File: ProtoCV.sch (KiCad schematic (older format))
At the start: 107 parts, among them J1 AudioJack2_SwitchT, J10 Conn_01x09_Male, J11 Conn_01x05_Male, J12 Conn_01x09_Male, J13 AudioJack2_SwitchT, J14 AudioJack2_SwitchT, J15 AudioJack2_SwitchT, J16 AudioJack2_SwitchT, J17 AudioJack2_SwitchT, J18 AudioJack2_SwitchT, J19 AudioJack2_SwitchT, J2 AudioJack2_SwitchT, J20 AudioJack2_SwitchT, J3 AudioJack2_SwitchT, J4 AudioJack2_SwitchT, J5 AudioJack2_SwitchT, J6 AudioJack2_SwitchT, J7 AudioJack2_SwitchT, J8 AudioJack2_SwitchT, J9 Conn_02x05_Odd_Even, U1 OPA4192, U2 OPA4192, U3 DC80508Z, U4 R-78E3.3-0.5, U5 LD2981ABU33TR, U6 74AHCT244, U7 L7805

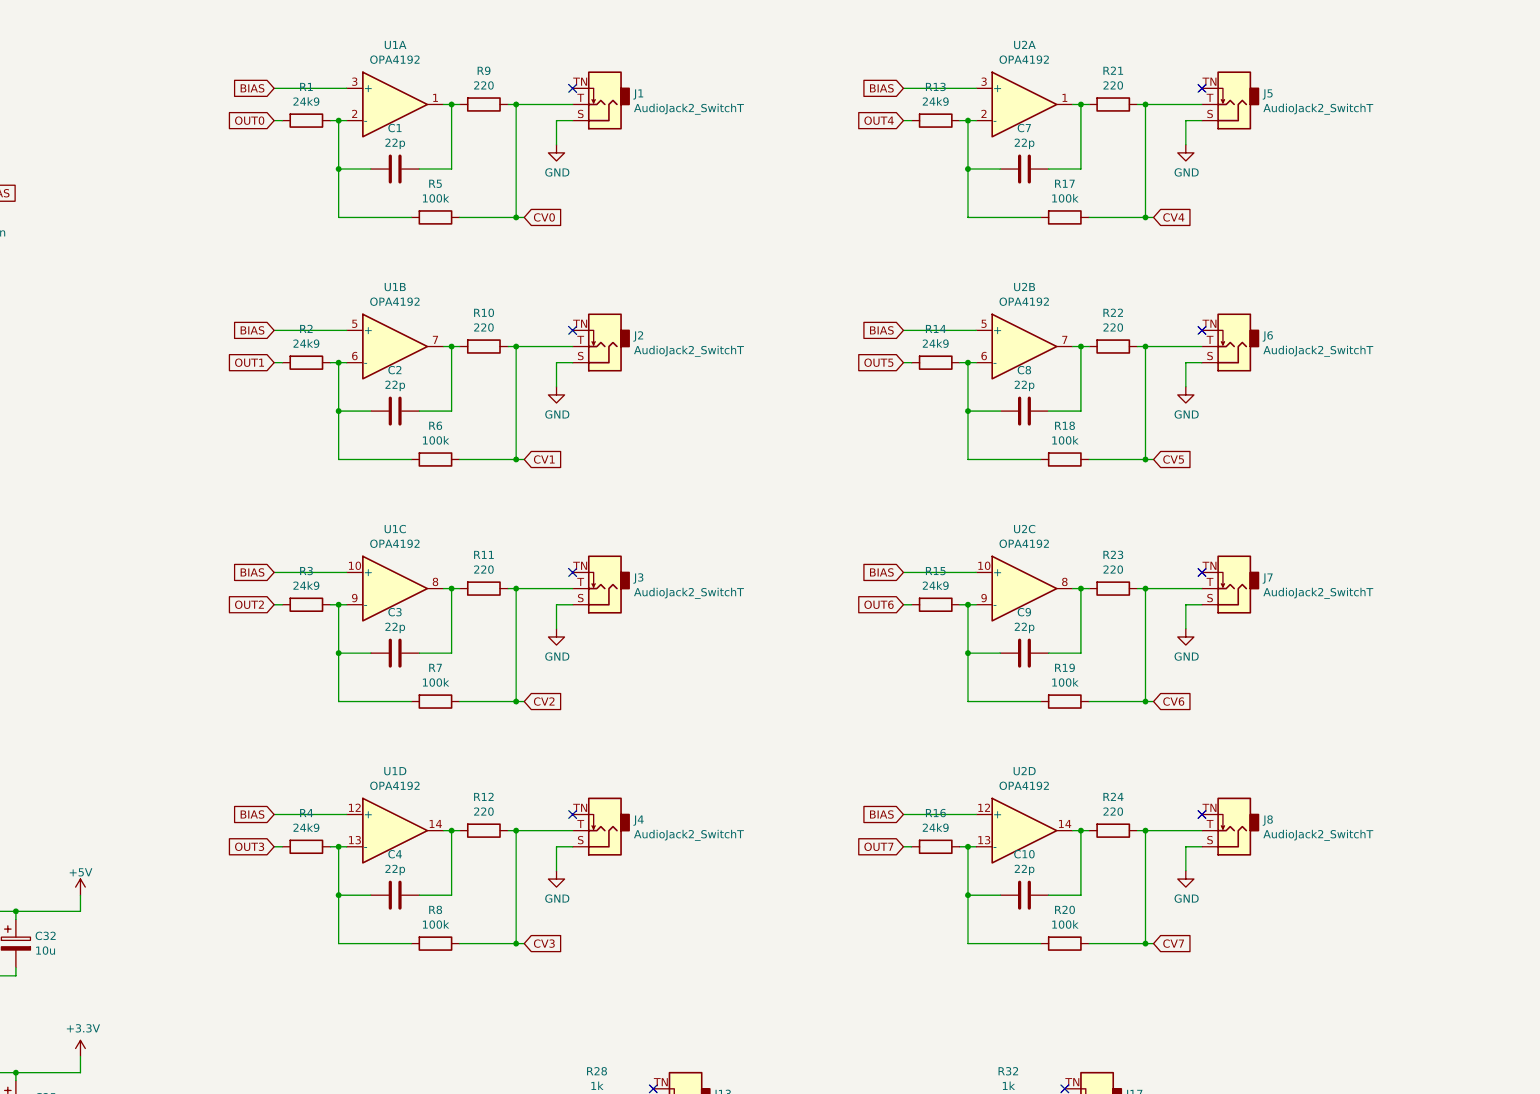
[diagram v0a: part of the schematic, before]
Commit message: Added leds and drivers.
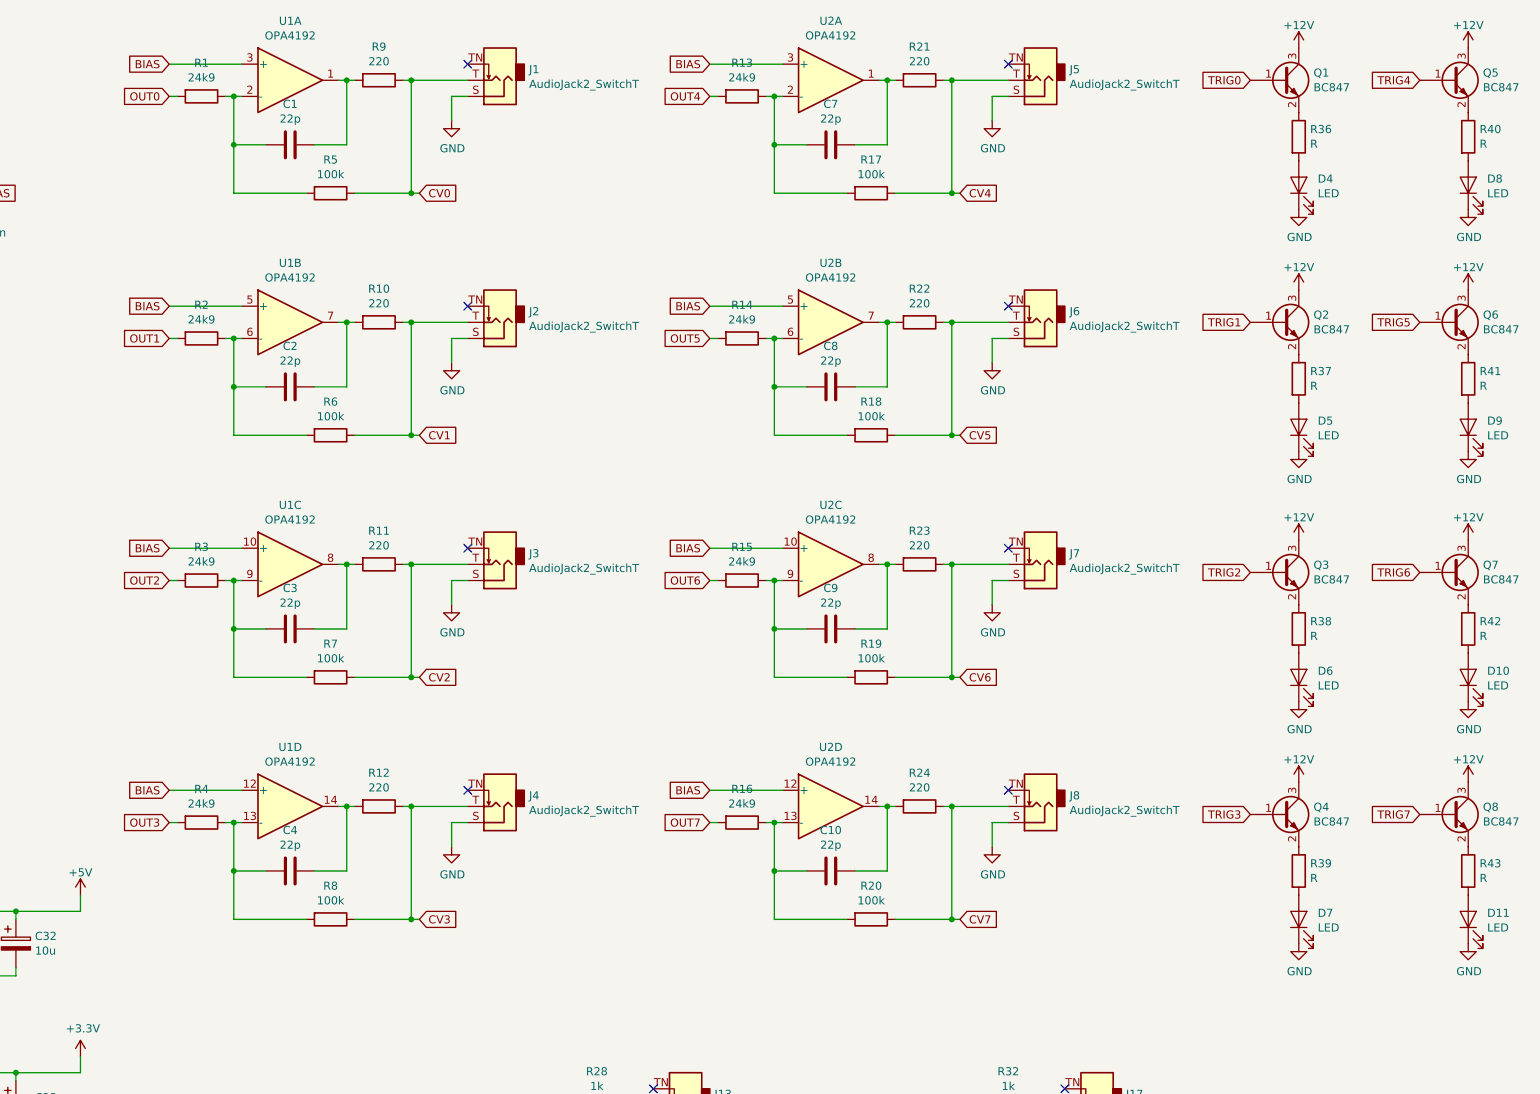
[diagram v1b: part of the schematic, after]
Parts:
- added D10, D11, D4, D5, D6, D7, D8, D9: LED, symbol Device:LED
- added Q1, Q2, Q3, Q4, Q5, Q6, Q7, Q8: BC847, Package_TO_SOT_SMD:SOT-23, symbol Transistor_BJT:BC847
- added R36, R37, R38, R39, R40, R41, R42, R43: R, symbol Device:R
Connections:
- net +12V: now also Q1.3 (C), Q2.3 (C), Q3.3 (C), Q4.3 (C), Q5.3 (C), Q6.3 (C), Q7.3 (C), Q8.3 (C)
- net GND: now also D10.1 (K), D11.1 (K), D4.1 (K), D5.1 (K), D6.1 (K), D7.1 (K), D8.1 (K), D9.1 (K)
- net TRIG0: now also Q1.1 (B)
- net TRIG1: now also Q2.1 (B)
- net TRIG2: now also Q3.1 (B)
- net TRIG3: now also Q4.1 (B)
- net TRIG4: now also Q5.1 (B)
- net TRIG5: now also Q6.1 (B)
- net TRIG6: now also Q7.1 (B)
- net TRIG7: now also Q8.1 (B)
- new net: Q1.2 (E), R36.1
- new net: D4.2 (A), R36.2
- new net: Q5.2 (E), R40.1
- new net: D8.2 (A), R40.2
- new net: Q2.2 (E), R37.1
- new net: D5.2 (A), R37.2
- new net: Q6.2 (E), R41.1
- new net: D9.2 (A), R41.2
- new net: Q3.2 (E), R38.1
- new net: D6.2 (A), R38.2
- new net: Q7.2 (E), R42.1
- new net: D10.2 (A), R42.2
- new net: Q4.2 (E), R39.1
- new net: D7.2 (A), R39.2
- new net: Q8.2 (E), R43.1
- new net: D11.2 (A), R43.2
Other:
- moved on the sheet: C1, C10, C2, C3, C4, C7, C8, C9, J1, J2, J3, J4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

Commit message: Assigned footprints.
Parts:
- C1, C10, C11, C12, C13, C14, C15, C2, C3, C4, C5, C6, C7, C8, C9: footprint (none) -> Capacitor_SMD:C_0603_1608Metric
- D10, D11, D4, D5, D6, D7, D8, D9: footprint (none) -> LED_SMD:LED_0603_1608Metric_Castellated
- H1, H2, H3, H4: footprint (none) -> MountingHole:MountingHole_3.2mm_M3_Pad_Via
- J1, J2, J3, J4, J5, J6, J7, J8: footprint (none) -> Local:PJ398SM
- J10, J12: footprint (none) -> Connector_PinHeader_2.54mm:PinHeader_1x09_P2.54mm_Vertical
- J11: footprint (none) -> Connector_PinHeader_2.54mm:PinHeader_1x05_P2.54mm_Vertical
- R1, R13, R14, R15, R16, R17, R18, R19, R2, R20, R25, R26, R3, R4, R5, R6, R7, R8: footprint (none) -> Resistor_SMD:R_0603_1608Metric
- R10, R11, R12, R21, R22, R23, R24, R9: footprint (none) -> Resistor_SMD:R_1206_3216Metric
- R36, R37, R38, R39, R40, R41, R42, R43: value R -> 47; footprint (none) -> Resistor_SMD:R_0603_1608Metric
- U1, U2: footprint (none) -> Package_SO:TSSOP-14_4.4x5mm_P0.65mm
- U3: value DC80508Z -> ADC80508Z; footprint (none) -> Package_DFN_QFN:QFN-16-1EP_3x3mm_P0.5mm_EP1.45x1.45mm_ThermalVias; symbol Local:DC80508Z -> Local:ADC80508Z

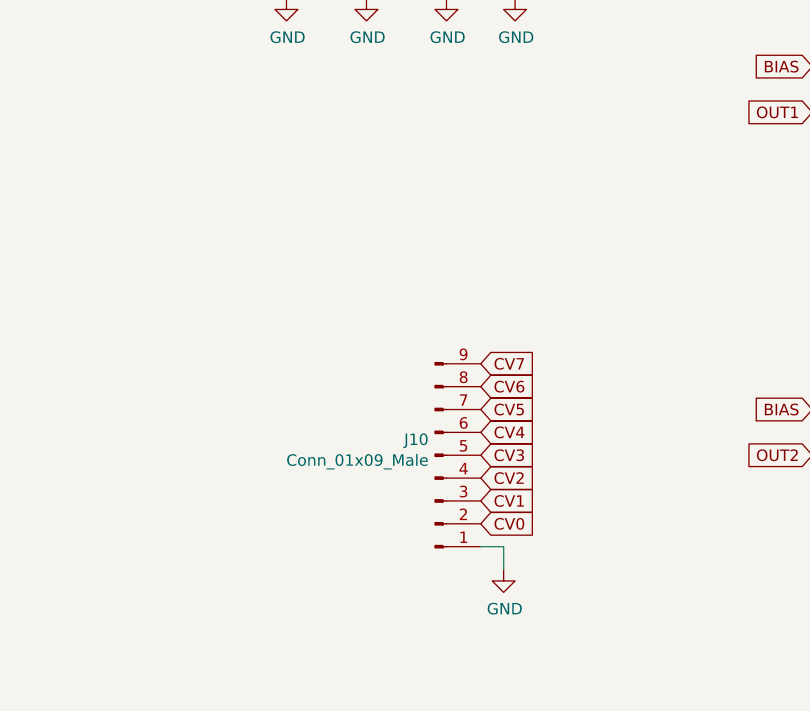
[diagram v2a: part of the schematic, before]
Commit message: Starting placement.
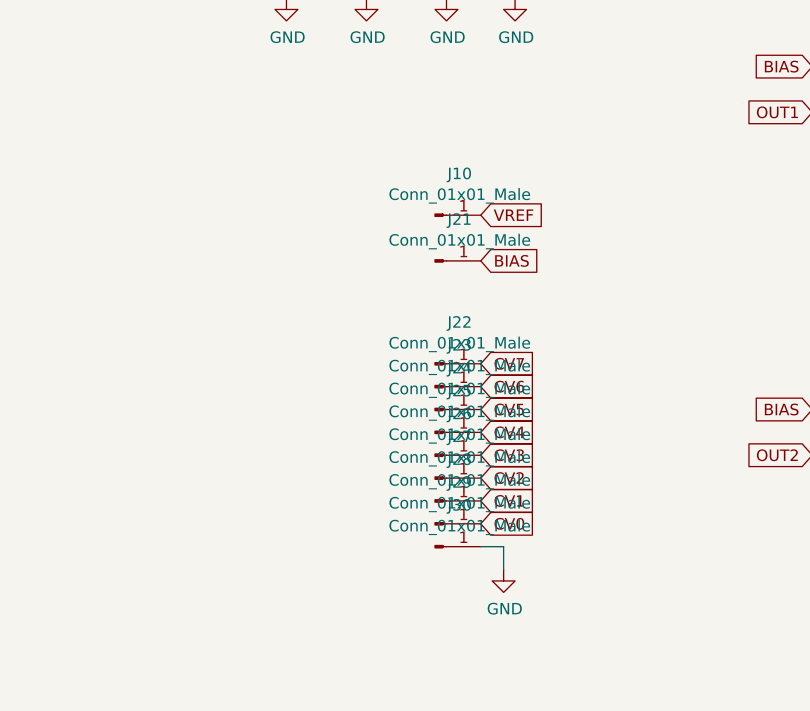
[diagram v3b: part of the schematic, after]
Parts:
- removed J10: Conn_01x09_Male, Connector_PinHeader_2.54mm:PinHeader_1x09_P2.54mm_Vertical, symbol Connector:Conn_01x09_Male
- added J10, J21, J22, J23, J24, J25, J26, J27, J28, J29, J30: Conn_01x01_Male, Connector_PinHeader_2.54mm:PinHeader_1x01_P2.54mm_Vertical, symbol Connector:Conn_01x01_Male
- J13, J14, J15, J16, J17, J18, J19, J20: footprint Local.pretty:PJ398SM -> Local:PJ398SM
- L1: footprint Inductor_SMD:L_0805_2012Metric -> Fuse:Fuse_Bourns_MF-RHT100
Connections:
- net BIAS: now also J21.1 (Pin_1)
- net CV0: now also J29.1 (Pin_1)
- net CV1: now also J28.1 (Pin_1)
- net CV2: now also J27.1 (Pin_1)
- net CV3: now also J26.1 (Pin_1)
- net CV4: now also J25.1 (Pin_1)
- net CV5: now also J24.1 (Pin_1)
- net CV6: now also J23.1 (Pin_1)
- net CV7: now also J22.1 (Pin_1)
- net GND: now also J30.1 (Pin_1)
- net VREF: now also J10.1 (Pin_1)
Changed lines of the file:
@@
 Connection ~ 12150 2100
-$Comp
-L Connector:Conn_01x09_Male J10
-U 1 1 5F278798
-P 5650 4500
-F 0 "J10" H 5622 4432 50  0000 R CNN
-F 1 "Conn_01x09_Male" H 5622 4523 50  0000 R CNN
-F 2 "Connector_PinHeader_2.54mm:PinHeader_1x09_P2.54mm_Vertical" H 5650 4500 50  0001 C CNN
-F 3 "~" H 5650 4500 50  0001 C CNN
-	1    5650 4500
-	1    0    0    1
-$EndComp
 $Comp
 L power:GND #PWR014
@@
 F 0 "L1" H 3900 7765 50  0000 C CNN
 F 1 "33u" H 3900 7674 50  0000 C CNN
-F 2 "Inductor_SMD:L_0805_2012Metric" H 3900 7550 50  0001 C CNN
+F 2 "Fuse:Fuse_Bourns_MF-RHT100" H 3900 7550 50  0001 C CNN
 F 3 "~" H 3900 7550 50  0001 C CNN
 	1    3900 7550
@@
 F 0 "J13" H 10321 7683 50  0000 R CNN
 F 1 "AudioJack2_SwitchT" H 10321 7774 50  0000 R CNN
-F 2 "Local.pretty:PJ398SM" H 10500 7750 50  0001 C CNN
+F 2 "Local:PJ398SM" H 10500 7750 50  0001 C CNN
 F 3 "~" H 10500 7750 50  0001 C CNN
 	1    10500 7750
@@
 F 0 "J14" H 10321 8133 50  0000 R CNN
 F 1 "AudioJack2_SwitchT" H 10321 8224 50  0000 R CNN
-F 2 "Local.pretty:PJ398SM" H 10500 8200 50  0001 C CNN
+F 2 "Local:PJ398SM" H 10500 8200 50  0001 C CNN
 F 3 "~" H 10500 8200 50  0001 C CNN
 	1    10500 8200
@@
 F 0 "J15" H 10321 8583 50  0000 R CNN
 F 1 "AudioJack2_SwitchT" H 10321 8674 50  0000 R CNN
-F 2 "Local.pretty:PJ398SM" H 10500 8650 50  0001 C CNN
+F 2 "Local:PJ398SM" H 10500 8650 50  0001 C CNN
 F 3 "~" H 10500 8650 50  0001 C CNN
 	1    10500 8650
@@
 F 0 "J16" H 10321 9033 50  0000 R CNN
 F 1 "AudioJack2_SwitchT" H 10321 9124 50  0000 R CNN
-F 2 "Local.pretty:PJ398SM" H 10500 9100 50  0001 C CNN
+F 2 "Local:PJ398SM" H 10500 9100 50  0001 C CNN
 F 3 "~" H 10500 9100 50  0001 C CNN
 	1    10500 9100
@@
 F 0 "J17" H 12871 7683 50  0000 R CNN
 F 1 "AudioJack2_SwitchT" H 12871 7774 50  0000 R CNN
-F 2 "Local.pretty:PJ398SM" H 13050 7750 50  0001 C CNN
+F 2 "Local:PJ398SM" H 13050 7750 50  0001 C CNN
 F 3 "~" H 13050 7750 50  0001 C CNN
 	1    13050 7750
@@
 F 0 "J18" H 12871 8133 50  0000 R CNN
 F 1 "AudioJack2_SwitchT" H 12871 8224 50  0000 R CNN
-F 2 "Local.pretty:PJ398SM" H 13050 8200 50  0001 C CNN
+F 2 "Local:PJ398SM" H 13050 8200 50  0001 C CNN
 F 3 "~" H 13050 8200 50  0001 C CNN
 	1    13050 8200
@@
 F 0 "J19" H 12871 8583 50  0000 R CNN
 F 1 "AudioJack2_SwitchT" H 12871 8674 50  0000 R CNN
-F 2 "Local.pretty:PJ398SM" H 13050 8650 50  0001 C CNN
+F 2 "Local:PJ398SM" H 13050 8650 50  0001 C CNN
 F 3 "~" H 13050 8650 50  0001 C CNN
 	1    13050 8650
@@
 F 0 "J20" H 12871 9033 50  0000 R CNN
 F 1 "AudioJack2_SwitchT" H 12871 9124 50  0000 R CNN
-F 2 "Local.pretty:PJ398SM" H 13050 9100 50  0001 C CNN
+F 2 "Local:PJ398SM" H 13050 9100 50  0001 C CNN
 F 3 "~" H 13050 9100 50  0001 C CNN
 	1    13050 9100
@@
 Text GLabel 15050 5950 0    50   Input ~ 0
 TRIG7
+$Comp
+L Connector:Conn_01x01_Male J22
+U 1 1 608E79F2
+P 5650 4100
+F 0 "J22" H 5758 4281 50  0000 C CNN
+F 1 "Conn_01x01_Male" H 5758 4190 50  0000 C CNN
+F 2 "Connector_PinHeader_2.54mm:PinHeader_1x01_P2.54mm_Vertical" H 5650 4100 50  0001 C CNN
+F 3 "~" H 5650 4100 50  0001 C CNN
+	1    5650 4100
+	1    0    0    -1
+$EndComp
+$Comp
+L Connector:Conn_01x01_Male J23
+U 1 1 608E967A
+P 5650 4200
+F 0 "J23" H 5758 4381 50  0000 C CNN
+F 1 "Conn_01x01_Male" H 5758 4290 50  0000 C CNN
+F 2 "Connector_PinHeader_2.54mm:PinHeader_1x01_P2.54mm_Vertical" H 5650 4200 50  0001 C CNN
+F 3 "~" H 5650 4200 50  0001 C CNN
+	1    5650 4200
+	1    0    0    -1
+$EndComp
+$Comp
+L Connector:Conn_01x01_Male J24
+U 1 1 608E9862
+P 5650 4300
+F 0 "J24" H 5758 4481 50  0000 C CNN
+F 1 "Conn_01x01_Male" H 5758 4390 50  0000 C CNN
+F 2 "Connector_PinHeader_2.54mm:PinHeader_1x01_P2.54mm_Vertical" H 5650 4300 50  0001 C CNN
+F 3 "~" H 5650 4300 50  0001 C CNN
+	1    5650 4300
+	1    0    0    -1
+$EndComp
+$Comp
+L Connector:Conn_01x01_Male J25
+U 1 1 608E9A83
+P 5650 4400
+F 0 "J25" H 5758 4581 50  0000 C CNN
+F 1 "Conn_01x01_Male" H 5758 4490 50  0000 C CNN
+F 2 "Connector_PinHeader_2.54mm:PinHeader_1x01_P2.54mm_Vertical" H 5650 4400 50  0001 C CNN
+F 3 "~" H 5650 4400 50  0001 C CNN
+	1    5650 4400
+	1    0    0    -1
+$EndComp
+$Comp
+L Connector:Conn_01x01_Male J26
+U 1 1 608E9C1A
+P 5650 4500
+F 0 "J26" H 5758 4681 50  0000 C CNN
+F 1 "Conn_01x01_Male" H 5758 4590 50  0000 C CNN
+F 2 "Connector_PinHeader_2.54mm:PinHeader_1x01_P2.54mm_Vertical" H 5650 4500 50  0001 C CNN
+F 3 "~" H 5650 4500 50  0001 C CNN
+	1    5650 4500
+	1    0    0    -1
+$EndComp
+$Comp
+L Connector:Conn_01x01_Male J27
+U 1 1 608E9F06
+P 5650 4600
+F 0 "J27" H 5758 4781 50  0000 C CNN
+F 1 "Conn_01x01_Male" H 5758 4690 50  0000 C CNN
+F 2 "Connector_PinHeader_2.54mm:PinHeader_1x01_P2.54mm_Vertical" H 5650 4600 50  0001 C CNN
+F 3 "~" H 5650 4600 50  0001 C CNN
+	1    5650 4600
+	1    0    0    -1
+$EndComp
+$Comp
+L Connector:Conn_01x01_Male J28
+U 1 1 608EA0EE
+P 5650 4700
+F 0 "J28" H 5758 4881 50  0000 C CNN
+F 1 "Conn_01x01_Male" H 5758 4790 50  0000 C CNN
+F 2 "Connector_PinHeader_2.54mm:PinHeader_1x01_P2.54mm_Vertical" H 5650 4700 50  0001 C CNN
+F 3 "~" H 5650 4700 50  0001 C CNN
+	1    5650 4700
+	1    0    0    -1
+$EndComp
+$Comp
+L Connector:Conn_01x01_Male J29
+U 1 1 608EA292
+P 5650 4800
+F 0 "J29" H 5758 4981 50  0000 C CNN
+F 1 "Conn_01x01_Male" H 5758 4890 50  0000 C CNN
+F 2 "Connector_PinHeader_2.54mm:PinHeader_1x01_P2.54mm_Vertical" H 5650 4800 50  0001 C CNN
+F 3 "~" H 5650 4800 50  0001 C CNN
+	1    5650 4800
+	1    0    0    -1
+$EndComp
+$Comp
+L Connector:Conn_01x01_Male J30
+U 1 1 608EA52D
+P 5650 4900
+F 0 "J30" H 5758 5081 50  0000 C CNN
+F 1 "Conn_01x01_Male" H 5758 4990 50  0000 C CNN
+F 2 "Connector_PinHeader_2.54mm:PinHeader_1x01_P2.54mm_Vertical" H 5650 4900 50  0001 C CNN
+F 3 "~" H 5650 4900 50  0001 C CNN
+	1    5650 4900
+	1    0    0    -1
+$EndComp
+$Comp
+L Connector:Conn_01x01_Male J21
+U 1 1 608EA6F6
+P 5650 3650
+F 0 "J21" H 5758 3831 50  0000 C CNN
+F 1 "Conn_01x01_Male" H 5758 3740 50  0000 C CNN
+F 2 "Connector_PinHeader_2.54mm:PinHeader_1x01_P2.54mm_Vertical" H 5650 3650 50  0001 C CNN
+F 3 "~" H 5650 3650 50  0001 C CNN
+	1    5650 3650
+	1    0    0    -1
+$EndComp
+Text GLabel 5850 3650 2    50   Input ~ 0
+BIAS
+$Comp
+L Connector:Conn_01x01_Male J10
+U 1 1 609123CA
+P 5650 3450
+F 0 "J10" H 5758 3631 50  0000 C CNN
+F 1 "Conn_01x01_Male" H 5758 3540 50  0000 C CNN
+F 2 "Connector_PinHeader_2.54mm:PinHeader_1x01_P2.54mm_Vertical" H 5650 3450 50  0001 C CNN
+F 3 "~" H 5650 3450 50  0001 C CNN
+	1    5650 3450
+	1    0    0    -1
+$EndComp
+Text GLabel 5850 3450 2    50   Input ~ 0
+VREF
 $EndSCHEMATC

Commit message: Completed placement.
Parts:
- L1: footprint Fuse:Fuse_Bourns_MF-RHT100 -> Inductor_SMD:L_0805_2012Metric
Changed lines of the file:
@@
 F 0 "L1" H 3900 7765 50  0000 C CNN
 F 1 "33u" H 3900 7674 50  0000 C CNN
-F 2 "Fuse:Fuse_Bourns_MF-RHT100" H 3900 7550 50  0001 C CNN
+F 2 "Inductor_SMD:L_0805_2012Metric" H 3900 7550 50  0001 C CNN
 F 3 "~" H 3900 7550 50  0001 C CNN
 	1    3900 7550

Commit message: Improved placement with separate analogue section.
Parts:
- added C34: 1n, Capacitor_SMD:C_0603_1608Metric, symbol Device:C
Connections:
- net +3.3VA: now also C34.1
- net GND: now also C34.2
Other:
- moved on the sheet: C33
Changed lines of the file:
@@
 	9200 10000 9200 10100
 Wire Wire Line
-	9750 10000 9750 10100
+	9750 10000 9750 10050
 $Comp
 L Mechanical:MountingHole H1
@@
 	3000 2900 3000 2650
 Wire Wire Line
-	9750 10400 9750 10500
+	9750 10400 9750 10450
 $Comp
 L Device:C C?
 U 1 1 6033C769
-P 10300 10250
+P 10800 10250
 AR Path="/5F2EFD7F/6033C769" Ref="C?"  Part="1"
 AR Path="/6033C769" Ref="C33"  Part="1"
-F 0 "C33" H 10415 10296 50  0000 L CNN
-F 1 "100n" H 10415 10205 50  0000 L CNN
-F 2 "Capacitor_SMD:C_0603_1608Metric" H 10338 10100 50  0001 C CNN
-F 3 "~" H 10300 10250 50  0001 C CNN
-	1    10300 10250
+F 0 "C33" H 10915 10296 50  0000 L CNN
+F 1 "100n" H 10915 10205 50  0000 L CNN
+F 2 "Capacitor_SMD:C_0603_1608Metric" H 10838 10100 50  0001 C CNN
+F 3 "~" H 10800 10250 50  0001 C CNN
+	1    10800 10250
 	1    0    0    -1
 $EndComp
@@
 L power:GND #PWR0102
 U 1 1 6033C773
-P 10300 10500
-F 0 "#PWR0102" H 10300 10250 50  0001 C CNN
-F 1 "GND" H 10305 10327 50  0000 C CNN
-F 2 "" H 10300 10500 50  0001 C CNN
-F 3 "" H 10300 10500 50  0001 C CNN
-	1    10300 10500
-	1    0    0    -1
-$EndComp
-Wire Wire Line
-	10300 10000 10300 10100
-Wire Wire Line
-	10300 10400 10300 10500
+P 10800 10500
+F 0 "#PWR0102" H 10800 10250 50  0001 C CNN
+F 1 "GND" H 10805 10327 50  0000 C CNN
+F 2 "" H 10800 10500 50  0001 C CNN
+F 3 "" H 10800 10500 50  0001 C CNN
+	1    10800 10500
+	1    0    0    -1
+$EndComp
+Wire Wire Line
+	10800 10000 10800 10100
+Wire Wire Line
+	10800 10400 10800 10500
 $Comp
 L power:+5V #PWR?
 U 1 1 60368A5E
-P 10300 10000
+P 10800 10000
 AR Path="/5FB86C29/60368A5E" Ref="#PWR?"  Part="1"
 AR Path="/60368A5E" Ref="#PWR0103"  Part="1"
-F 0 "#PWR0103" H 10300 9850 50  0001 C CNN
-F 1 "+5V" H 10315 10173 50  0000 C CNN
-F 2 "" H 10300 10000 50  0001 C CNN
-F 3 "" H 10300 10000 50  0001 C CNN
-	1    10300 10000
+F 0 "#PWR0103" H 10800 9850 50  0001 C CNN
+F 1 "+5V" H 10815 10173 50  0000 C CNN
+F 2 "" H 10800 10000 50  0001 C CNN
+F 3 "" H 10800 10000 50  0001 C CNN
+	1    10800 10000
 	1    0    0    -1
 $EndComp
@@
 Text GLabel 5850 3450 2    50   Input ~ 0
 VREF
+$Comp
+L Device:C C?
+U 1 1 60F19883
+P 10150 10250
+AR Path="/5F2EFD7F/60F19883" Ref="C?"  Part="1"
+AR Path="/60F19883" Ref="C34"  Part="1"
+F 0 "C34" H 10265 10296 50  0000 L CNN
+F 1 "1n" H 10265 10205 50  0000 L CNN
+F 2 "Capacitor_SMD:C_0603_1608Metric" H 10188 10100 50  0001 C CNN
+F 3 "~" H 10150 10250 50  0001 C CNN
+	1    10150 10250
+	1    0    0    -1
+$EndComp
+Wire Wire Line
+	9750 10050 10150 10050
+Wire Wire Line
+	10150 10050 10150 10100
+Connection ~ 9750 10050
+Wire Wire Line
+	9750 10050 9750 10100
+Wire Wire Line
+	9750 10450 10150 10450
+Wire Wire Line
+	10150 10450 10150 10400
+Connection ~ 9750 10450
+Wire Wire Line
+	9750 10450 9750 10500
 $EndSCHEMATC
